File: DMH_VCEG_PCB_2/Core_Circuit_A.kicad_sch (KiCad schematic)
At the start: 84 parts, among them J22 Conn_01x10_PinHeader, Q1 BC548, Q2 BC558, Q3 BC548, SW1 SW_DPDT_x2, U1 TL074, U2 4001, U3 40106, U4 CD4066BE, U5 TL074, U6 TL074, U7 TL074

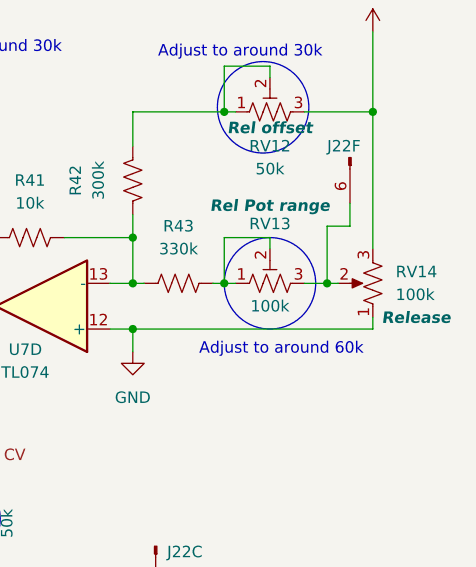
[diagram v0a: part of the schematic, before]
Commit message: Placed front panel components on PCB 2
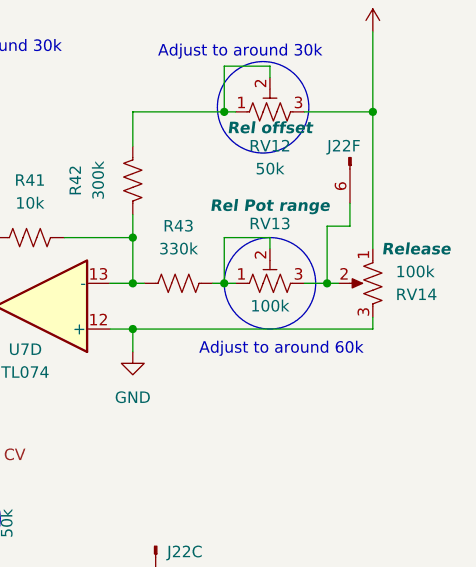
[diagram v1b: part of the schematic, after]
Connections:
- net +12V: now also RV14.1; no longer RV14.3
- net GND: now also RV14.3; no longer RV14.1
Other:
- moved on the sheet: RV14

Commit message: Placed ICs and pin headers on PCB 2
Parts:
- J22: footprint (none) -> Connector_PinSocket_2.54mm:PinSocket_1x10_P2.54mm_Vertical
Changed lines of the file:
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@@
 			)
 		)
-		(property "Footprint" ""
+		(property "Footprint" "Connector_PinSocket_2.54mm:PinSocket_1x10_P2.54mm_Vertical"
 			(at 127 157.48 0)
 			(effects
@@
 			)
 		)
-		(property "Footprint" ""
+		(property "Footprint" "Connector_PinSocket_2.54mm:PinSocket_1x10_P2.54mm_Vertical"
 			(at 251.46 76.2 0)
 			(effects
@@
 			)
 		)
-		(property "Footprint" ""
+		(property "Footprint" "Connector_PinSocket_2.54mm:PinSocket_1x10_P2.54mm_Vertical"
 			(at 185.42 133.35 0)
 			(effects
@@
 		(exclude_from_sim no)
 		(in_bom yes)
-		(on_board yes)
+		(on_board no)
 		(dnp no)
 		(property "Reference" "U1"
@@
 		(exclude_from_sim no)
 		(in_bom yes)
-		(on_board yes)
+		(on_board no)
 		(dnp no)
 		(property "Reference" "U1"
@@
 			)
 		)
-		(property "Footprint" ""
+		(property "Footprint" "Connector_PinSocket_2.54mm:PinSocket_1x10_P2.54mm_Vertical"
 			(at 151.13 193.04 0)
 			(effects
@@
 			)
 		)
-		(property "Footprint" ""
+		(property "Footprint" "Connector_PinSocket_2.54mm:PinSocket_1x10_P2.54mm_Vertical"
 			(at 273.05 33.02 0)
 			(effects

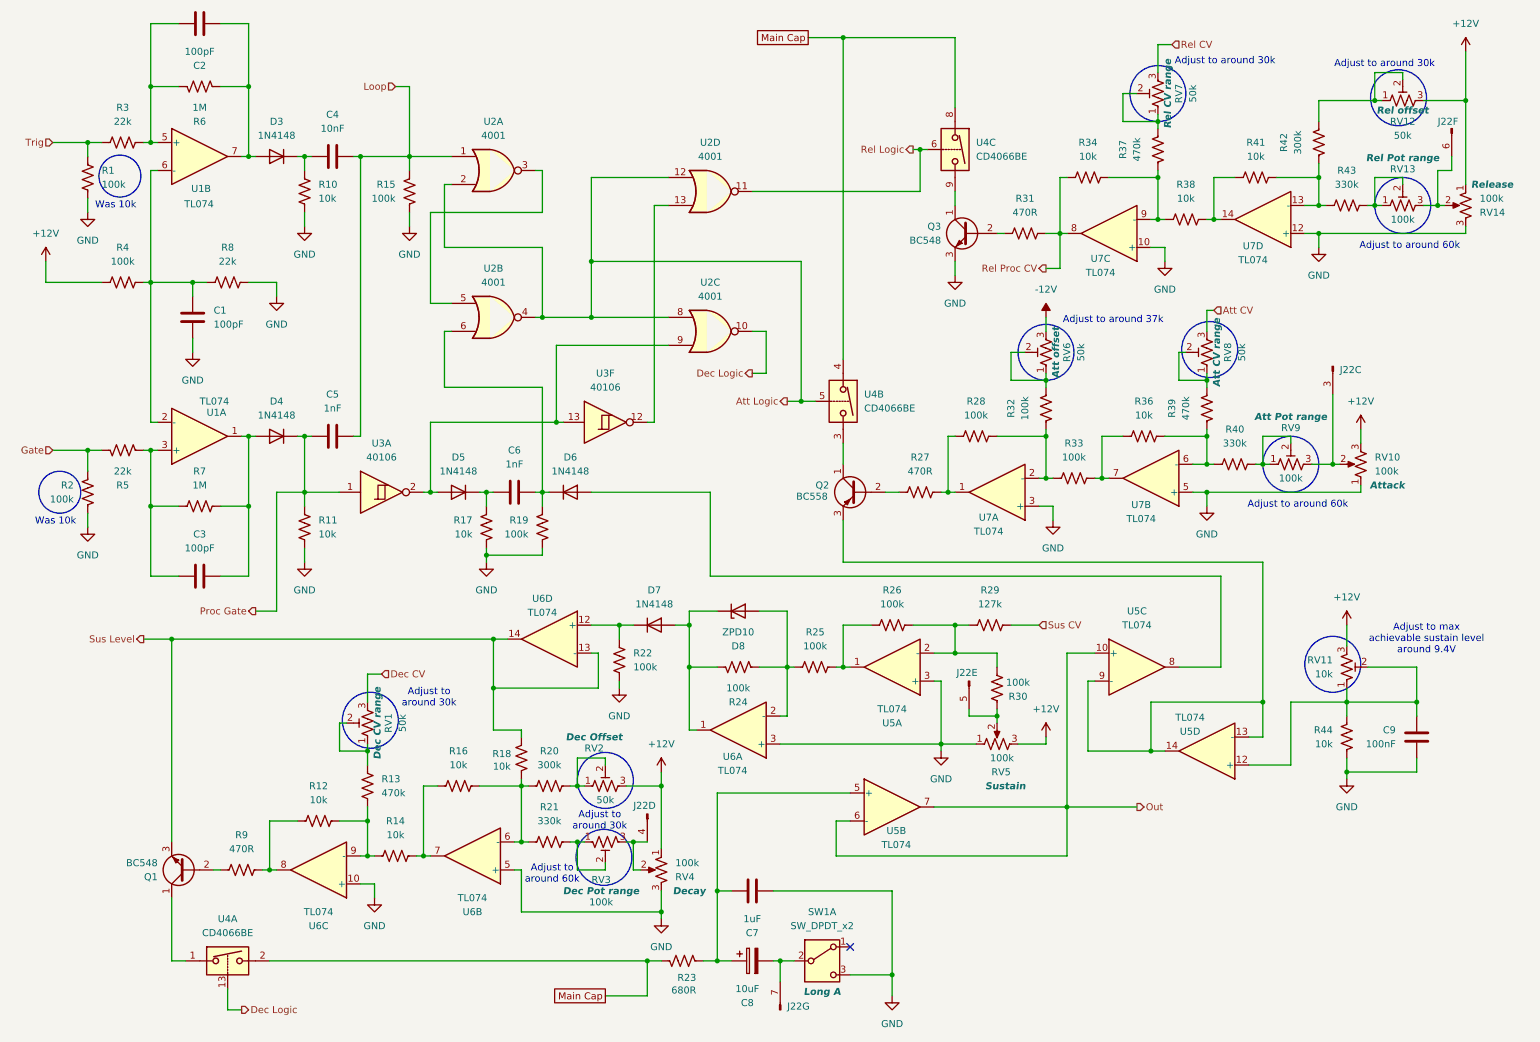
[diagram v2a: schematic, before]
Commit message: Added Output attenuation circuit
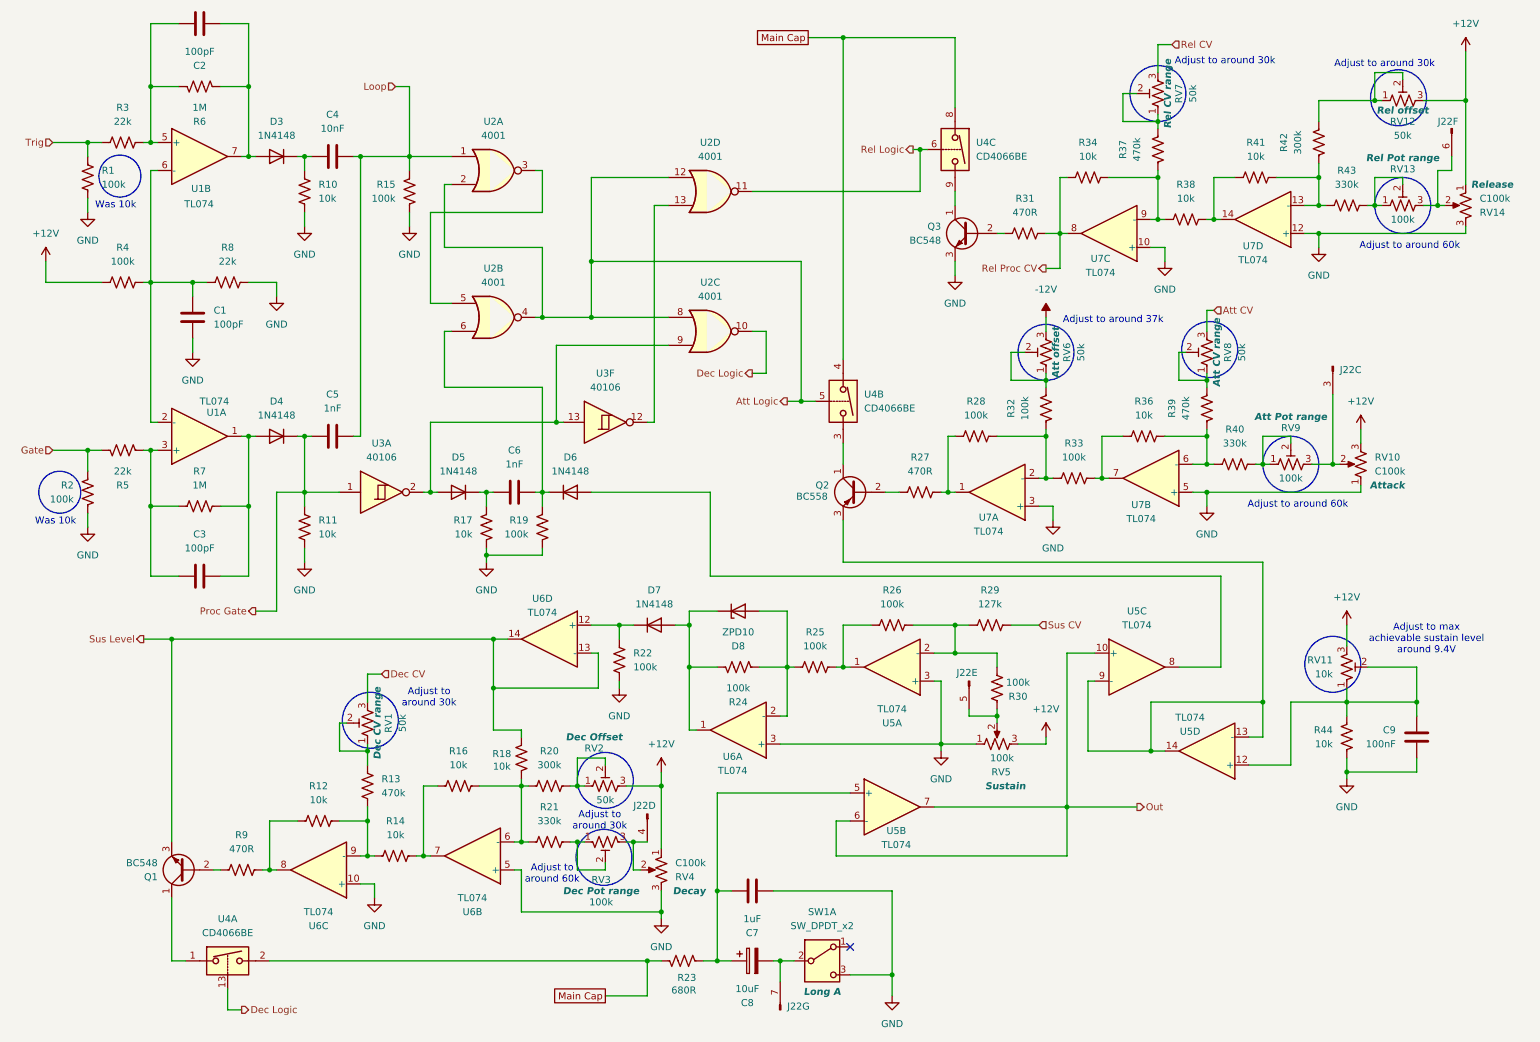
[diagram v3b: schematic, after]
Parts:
- RV10, RV14, RV4: value 100k -> C100k
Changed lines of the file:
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@@
 			)
 		)
-		(property "Value" "100k"
+		(property "Value" "C100k"
 			(at 132.08 166.3701 0)
 			(effects
@@
 			)
 		)
-		(property "Value" "100k"
+		(property "Value" "C100k"
 			(at 259.08 95.2499 0)
 			(effects
@@
 			)
 		)
-		(property "Value" "100k"
+		(property "Value" "C100k"
 			(at 278.13 45.7201 0)
 			(effects

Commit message: Removed unnecessary trimpots
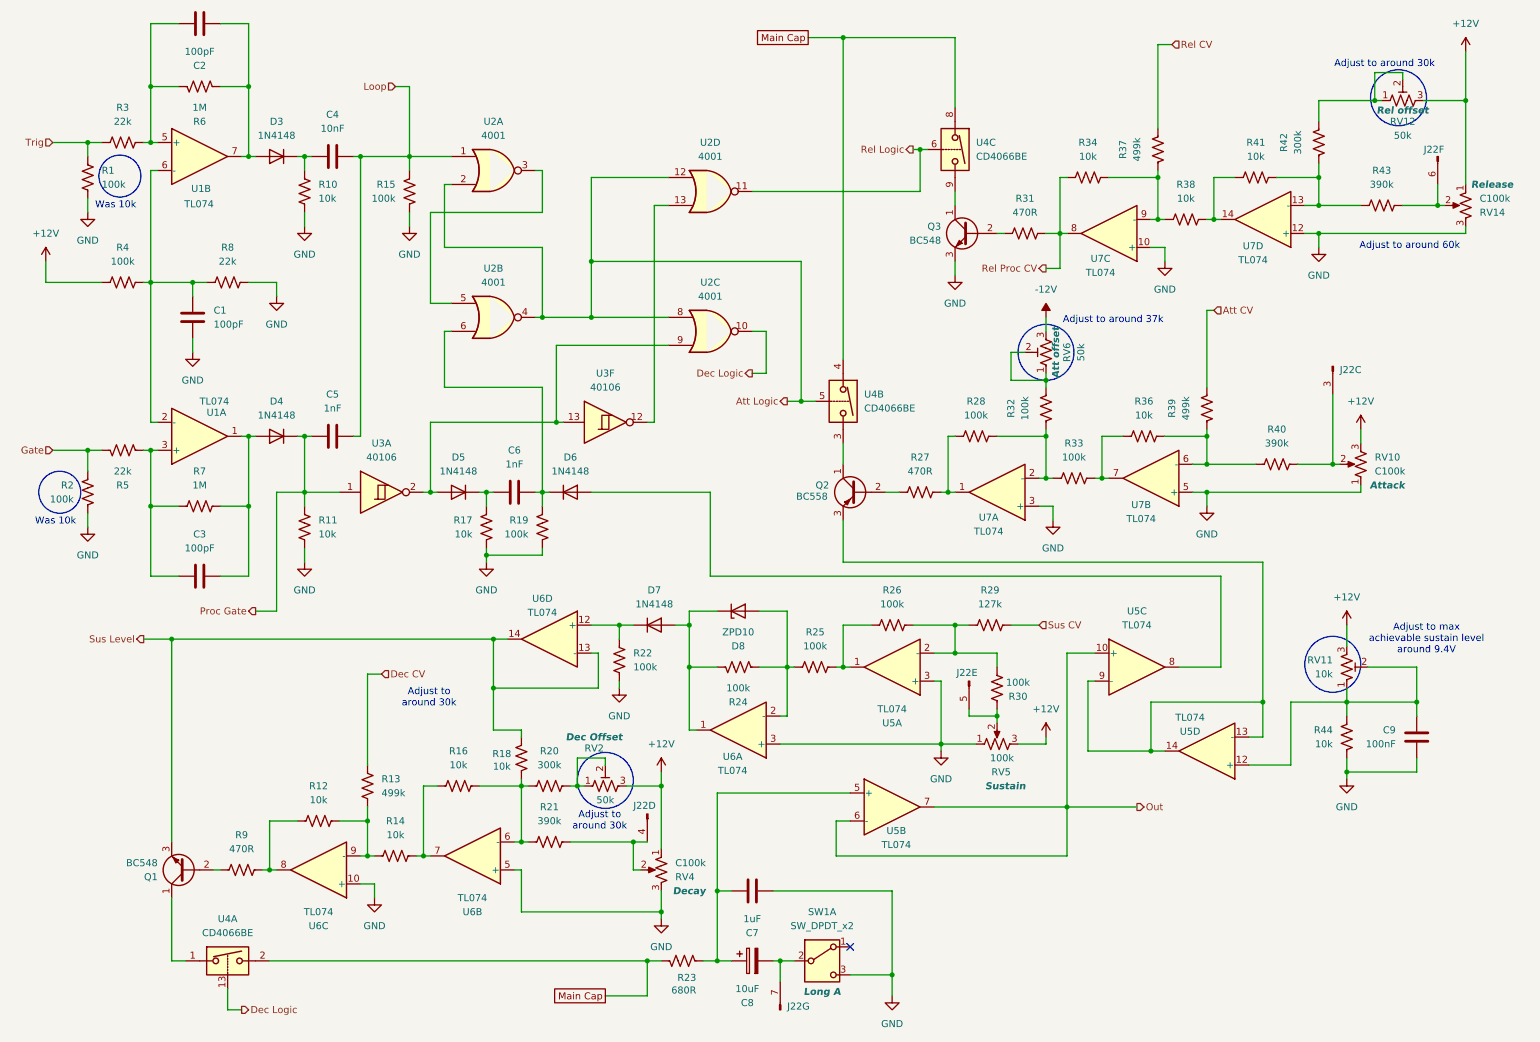
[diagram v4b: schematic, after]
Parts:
- removed RV1, RV7, RV8: 50k, Potentiometer_THT:Potentiometer_Bourns_3296W_Vertical, symbol Device:R_Potentiometer_Trim_US
- removed RV13, RV3, RV9: 100k, Potentiometer_THT:Potentiometer_Bourns_3296W_Vertical, symbol Device:R_Potentiometer_Trim_US
- R13, R37, R39: value 470k -> 499k
- R21, R40, R43: value 330k -> 390k
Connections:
- net Att CV: now also R39.2
- net Dec CV: now also R13.2
- net Rel CV: now also R37.2
- net at R40.1: now also J22.3 (Pin_3), RV10.2
- net at R43.1: now also J22.6 (Pin_6), RV14.2
- net at J22.4 (Pin_4), RV4.2: now also R21.1
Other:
- moved on the sheet: J22F, R40, R43
